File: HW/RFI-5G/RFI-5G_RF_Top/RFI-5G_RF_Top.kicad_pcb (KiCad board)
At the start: 2 copper layers, 40 x 40 mm, 36 parts, among them J1 Conn_01x03, J2 Conn_01x02, J3 Conn_01x06_Female, J4 Conn_01x03, J5 SMP, J6 Conn_01x10, U1 HMC342, U2 HMC342, U3 HMC260, U4 CY2-44+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

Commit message: PL boards
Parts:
- removed J2: Conn_01x02, Connector_PinHeader_2.54mm:PinHeader_1x02_P2.54mm_Vertical
- removed J3: Conn_01x06_Female, Connector_PinHeader_1.00mm:PinHeader_1x06_P1.00mm_Vertical
- removed J4: Conn_01x03, Connector_PinHeader_2.54mm:PinHeader_1x03_P2.54mm_Vertical
- removed J6: Conn_01x10, Connector_PinHeader_2.54mm:PinHeader_1x10_P2.54mm_Vertical
- added REF**: OSHW-Symbol_6.7x6mm_SilkScreen, Symbol:OSHW-Symbol_6.7x6mm_SilkScreen, F.Cu at (120.0, 119.0)
- J1: value Conn_01x03 -> Conn_01x09_Female; footprint Connector_PinHeader_2.54mm:PinHeader_1x03_P2.54mm_Vertical -> Connector_PinSocket_1.00mm:PinSocket_1x09_P1.00mm_Vertical
- moved C15 56.5 mm to (151.1, 98.8)
- moved U6 55.5 mm to (150.7, 97.1), turned to 180 degrees
- moved C14 42.0 mm to (132.2, 101.6), turned to 180 degrees
- moved C13 40.8 mm to (132.2, 100.5), turned to 180 degrees
- moved C10 40.2 mm to (132.2, 103.8), turned to 180 degrees
- moved C9 38.9 mm to (132.2, 102.7), turned to 180 degrees
- moved C8 38.6 mm to (132.2, 106.0), turned to 180 degrees
- moved C7 37.2 mm to (132.2, 104.9), turned to 180 degrees
- moved U5 35.5 mm to (128.8, 96.8), turned to 90 degrees
- moved R1 31.2 mm to (129.0, 101.1), turned to 90 degrees
- moved C11 31.0 mm to (133.0, 109.2), turned to 90 degrees
- moved R3 30.0 mm to (127.4, 100.6), turned to 180 degrees
- moved C12 29.7 mm to (132.0, 109.2), turned to 90 degrees
- moved R2 29.0 mm to (127.4, 101.6), turned to 180 degrees
- moved U4 28.0 mm to (129.0, 104.4), turned to 180 degrees
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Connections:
- C1 pad 1: Vcc_LNA -> Vcc_LNA1
- C2 pad 1: Vcc_LNA -> Vcc_LNA1
- C3 pad 1: Vcc_LNA -> Vcc_LNA1
- C4 pad 1: Vcc_LNA -> Vcc_LNA2
- C5 pad 1: Vcc_LNA -> Vcc_LNA2
- C6 pad 1: Vcc_LNA -> Vcc_LNA2
- J1 pad 1: SDA -> VTune1
- J1 pad 2: SCL -> Vcc_VCO
- J1 pad 3: GND -> Vcc_LO1Amp
- U1 pad 21: Vcc_LNA -> Vcc_LNA1
- U2 pad 21: Vcc_LNA -> Vcc_LNA2
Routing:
- net Vcc_LO1Amp: track 0.00 -> 68.3 mm, vias 0 -> 1
- net VTune1: track 0.00 -> 60.5 mm, vias 0 -> 1
- net Vcc_VCO: track 0.00 -> 57.5 mm, vias 0 -> 1
- net Vcc_LNA1: track 0.00 -> 13.8 mm
- net Vcc_LNA2: track 0.00 -> 10.7 mm
- net 3V: track 0.00 -> 10.5 mm
- net SCL: track 0.00 -> 7.07 mm
- net SDA: track 0.00 -> 6.46 mm
- net GND: track 0.00 -> 1.60 mm, vias 0 -> 1
- added copper zone on B.Cu, net GND
- added copper zone on F.Cu, net GND
- removed copper zone on B.Cu, net (none)
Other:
- board text added: "Custom top structural part, includes RF shield plus lateral mounting holes"

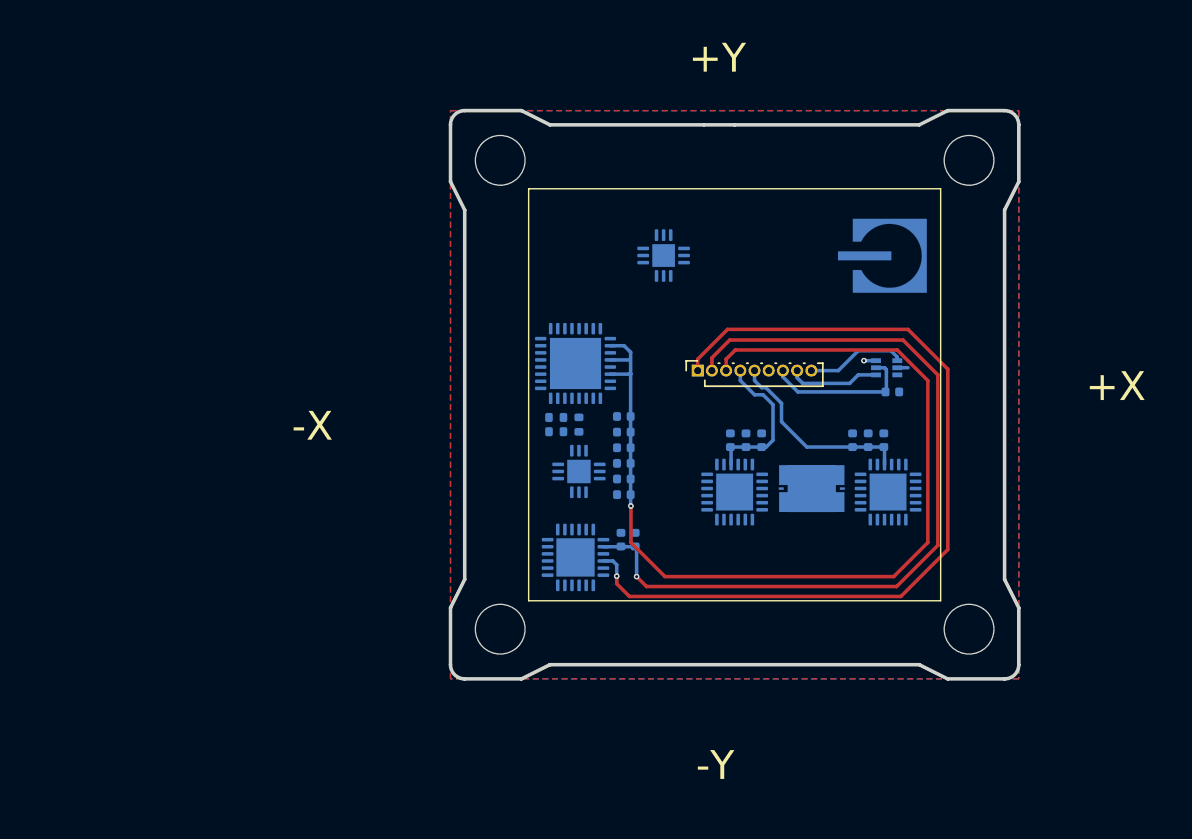
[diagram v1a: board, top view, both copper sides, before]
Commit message: All boards dseigned, thickness change pending
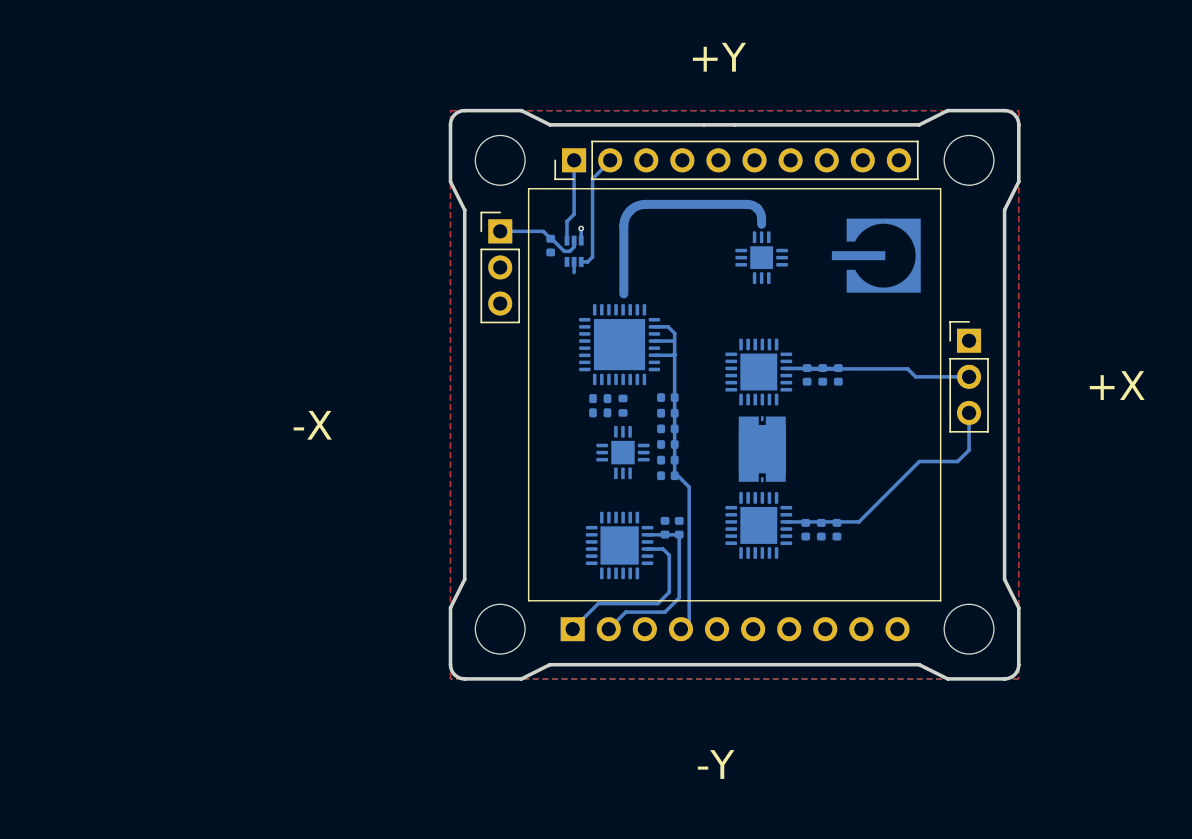
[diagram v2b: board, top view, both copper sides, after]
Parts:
- added J2: Conn_01x03, Connector_PinHeader_2.54mm:PinHeader_1x03_P2.54mm_Vertical, F.Cu at (156.5, 95.2)
- added J3: Conn_01x03, Connector_PinHeader_2.54mm:PinHeader_1x03_P2.54mm_Vertical, F.Cu at (123.5, 87.5)
- added J4: Conn_01x10, Connector_PinHeader_2.54mm:PinHeader_1x10_P2.54mm_Vertical, B.Cu at (128.6, 115.5)
- J1: value Conn_01x09_Female -> Conn_01x10; footprint Connector_PinSocket_1.00mm:PinSocket_1x09_P1.00mm_Vertical -> Connector_PinHeader_2.54mm:PinHeader_1x10_P2.54mm_Vertical
- moved C15 26.2 mm to (127.0, 88.5), turned to 90 degrees
- moved U6 23.5 mm to (128.7, 88.9), turned to 90 degrees
- moved J1 17.2 mm to (128.7, 82.5)
- moved U1 9.40 mm to (141.7, 108.2), turned to 90 degrees
- moved C6 8.88 mm to (147.3, 97.6), turned to -90 degrees
- moved FL1 8.74 mm to (139.6, 105.4), turned to 90 degrees
- moved U2 8.62 mm to (141.7, 97.4), turned to 90 degrees
- moved C1 8.36 mm to (145.0, 108.5), turned to -90 degrees
- moved C2 7.11 mm to (146.1, 108.5), turned to -90 degrees
- moved C5 7.09 mm to (146.2, 97.6), turned to -90 degrees
- moved U3 6.90 mm to (141.9, 89.3)
- moved C3 6.40 mm to (147.2, 108.5), turned to -90 degrees
- moved C4 5.60 mm to (145.1, 97.6), turned to -90 degrees
- moved C10 3.37 mm to (135.3, 102.5)
- moved C13 3.37 mm to (135.3, 99.2)
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- renumbered J5 to J6
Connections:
- J1 pad 1: VTune1 -> SDA
- J1 pad 2: Vcc_VCO -> SCL
- J1 pad 3: Vcc_LO1Amp -> GND
- J1 pad 4: Vcc_LNA2 -> unconnected-(J1-Pad4)
- J1 pad 5: Vcc_LNA1 -> unconnected-(J1-Pad5)
- J1 pad 6: GND -> unconnected-(J1-Pad6)
- J1 pad 7: 3V -> unconnected-(J1-Pad7)
- J1 pad 8: SDA -> unconnected-(J1-Pad8)
- J1 pad 9: SCL -> unconnected-(J1-Pad9)
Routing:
- net VTune1: track 60.5 -> 12.2 mm, vias 1 -> 0
- net Vcc_VCO: track 57.5 -> 12.6 mm, vias 1 -> 0
- net Vcc_LO1Amp: track 68.3 -> 25.9 mm, vias 1 -> 0
- net (no net): track 0.00 -> 16.3 mm
- net Vcc_LNA2: track 10.7 -> 15.0 mm
- net 3V: track 10.5 -> 6.35 mm
- net Vcc_LNA1: track 13.8 -> 17.6 mm
- net SCL: track 7.07 -> 8.26 mm
- net SDA: track 6.46 -> 5.86 mm
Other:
- board text added: "RO4350B thickness = 0.3 mm Er = 3.66 tand = 37e-4"

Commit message: almost finished PCB's
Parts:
- J1, J2, J3: moved to B.Cu
- moved C1 1.00 mm to (145.0, 109.5)
- moved C10 1.00 mm to (135.3, 103.5)
- moved C11 1.00 mm to (136.1, 109.4)
- moved C12 1.00 mm to (135.1, 109.4)
- moved C13 1.00 mm to (135.3, 100.2)
- moved C14 1.00 mm to (135.3, 101.3)
- moved C15 1.00 mm to (127.0, 89.5)
- moved C2 1.00 mm to (146.1, 109.5)
- moved C3 1.00 mm to (147.2, 109.5)
- moved C7 1.00 mm to (135.3, 104.6)
- moved C8 1.00 mm to (135.3, 105.7)
- moved C9 1.00 mm to (135.3, 102.4)
- moved H1 1.00 mm to (123.5, 83.5)
- moved H2 1.00 mm to (156.5, 83.5)
- moved H3 1.00 mm to (123.5, 116.5)
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- gave numbers to parts that had none: 4
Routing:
- net LO1: track 0.00 -> 17.5 mm
- net (no net): track 16.3 -> 0.00 mm
- net IF1_In: track 0.00 -> 5.28 mm
- net /RF_LNA2_Out: track 0.00 -> 4.22 mm
- net /VCO1_Out: track 0.00 -> 3.06 mm
- net Vcc_LNA2: track 15.0 -> 13.2 mm
- net /Att_Out: track 0.00 -> 1.75 mm
- net /Mult_Out: track 0.00 -> 1.75 mm
- net /RF_LNA1_Out: track 0.00 -> 1.54 mm
- net /RF_FL_Out: track 0.00 -> 1.08 mm
- net GND: vias 1 -> 209
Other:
- outline, holes or cut-outs redrawn
